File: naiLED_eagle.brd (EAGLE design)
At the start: 12.4 x 12.7 mm, 9 parts, among them IC1 TCS3414, U2 24LC00T-I/OT, U3 ATTINY25-20SSU

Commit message: miniSK led
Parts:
- removed LED1: LED_RGB3, dp_devices:RGBLED
- added U$1: SK6812MINI, pimoroni-optoelectronics:LED-3535
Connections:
- net D1/PWM/MISO: no longer LED1.AG
- net D3/A3: no longer LED1.AR
- net D4/PWM: no longer LED1.AB
- net GND: now also U$1.1; no longer LED1.CB, LED1.CG, LED1.CR
- net VCC: now also U$1.3
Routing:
- net VCC: track 37.9 -> 39.3 mm
- net D4/PWM: track 18.7 -> 18.0 mm
- net GND: vias 5 -> 1
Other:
- board text removed: "LED"

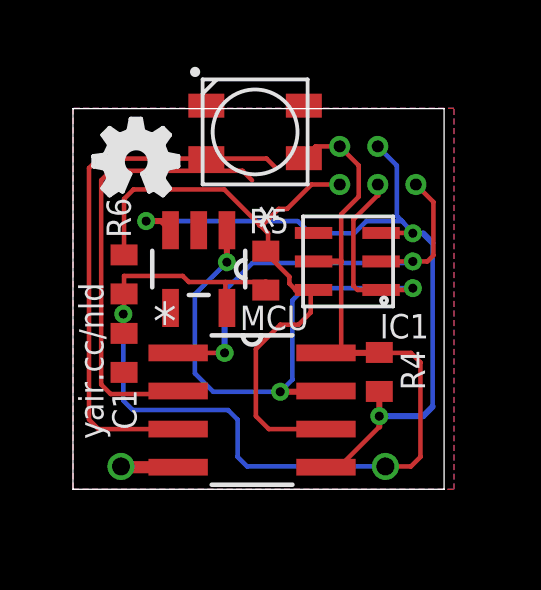
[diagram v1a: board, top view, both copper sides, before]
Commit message: changed attiny25 footprint to 85, ripup
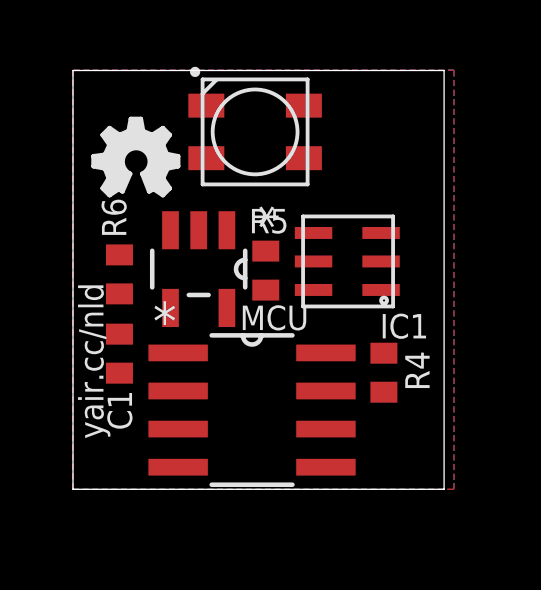
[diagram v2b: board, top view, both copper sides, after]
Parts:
- moved R4 0.15 mm to (10.4, 3.89)
- moved C1 0.15 mm to (1.55, 4.52)
- moved R6 0.15 mm to (1.55, 7.16)
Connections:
- net D4/PWM: now also U$1.2
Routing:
- net VCC: track 39.3 -> 0.00 mm, vias 3 -> 0
- net D0/PWM/MOSI/SDA: track 26.0 -> 0.00 mm, vias 4 -> 0
- net D2/A1/SCK/SCL: track 23.1 -> 0.00 mm, vias 4 -> 0
- net D1/PWM/MISO: track 21.4 -> 0.00 mm, vias 1 -> 0
- net D4/PWM: track 18.0 -> 0.00 mm
- net D3/A3: track 14.9 -> 0.00 mm
- net D5/A0/RESET: track 14.8 -> 0.00 mm, vias 3 -> 0
- net GND: track 1.50 -> 0.00 mm, vias 1 -> 0
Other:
- board size 12.4 x 12.7 mm -> 12.4 x 14 mm

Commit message: routing mid
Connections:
- removed net D5/A0/RESET: IC1.P$2, U3.1
- net D3/A3: now also IC1.P$2
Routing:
- net D0/PWM/MOSI/SDA: track 0.00 -> 25.9 mm
- net D2/A1/SCK/SCL: track 0.00 -> 15.8 mm
- net D4/PWM: track 0.00 -> 12.2 mm, vias 0 -> 2
- net VCC: track 0.00 -> 10.9 mm
- net GND: track 0.00 -> 10.1 mm
- net D1/PWM/MISO: track 0.00 -> 6.97 mm, vias 0 -> 2
- net D3/A3: track 0.00 -> 6.18 mm

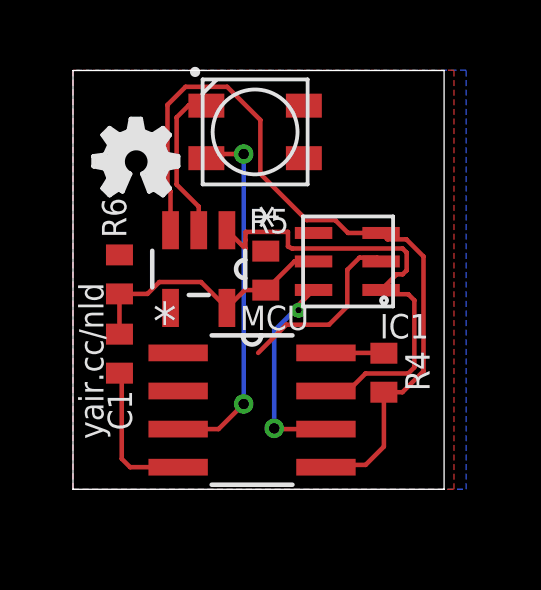
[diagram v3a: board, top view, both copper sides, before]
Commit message: ripup all, added vias to attiny
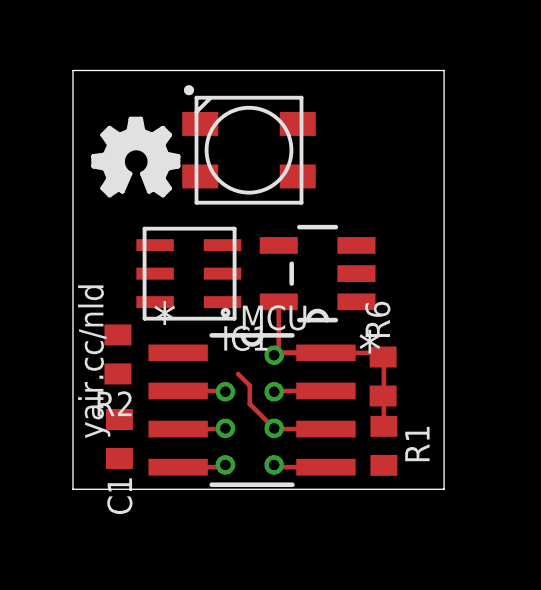
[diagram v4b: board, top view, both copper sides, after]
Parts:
- removed R4, R5: (no value), dp_devices:R402
- added R1, R2: (no value), dp_devices:R402
- moved R6 9.42 mm to (10.3, 3.76)
- moved IC1 5.30 mm to (3.89, 7.19)
- moved U2 3.97 mm to (8.15, 7.19), turned to 180 degrees
- moved C1 2.84 mm to (1.55, 1.68)
- moved U$1 0.64 mm to (5.87, 11.3)
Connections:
- new net NC: U3.1
- net D0/PWM/MOSI/SDA: now also R1.1; no longer R4.1
- net D1/PWM/MISO: now also R2.1; no longer R5.1
- net VCC: now also R1.2, R2.2; no longer R4.2, R5.2
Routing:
- net D0/PWM/MOSI/SDA: track 25.9 -> 1.80 mm, vias 0 -> 1
- net D2/A1/SCK/SCL: track 15.8 -> 1.75 mm, vias 0 -> 1
- net D4/PWM: track 12.2 -> 1.60 mm, vias 2 -> 1
- net GND: track 10.1 -> 1.65 mm, vias 0 -> 1
- net D3/A3: track 6.18 -> 1.60 mm, vias 0 -> 1
- net D1/PWM/MISO: track 6.97 -> 4.07 mm, vias 2 -> 1
- net VCC: track 10.9 -> 9.46 mm, vias 0 -> 1
- removed copper zone on layer 1, net GND
- removed copper zone on layer 16, net GND

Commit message: mem docs
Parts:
- removed C1: (no value), dp_devices:C402
- removed IC1: TCS3414, yair_r:DFN-6PIN
- removed R6: (no value), dp_devices:R402
- added C2: (no value), naiLED_eagle:C402
- added U$2: VEML6040, naiLED_eagle:4-TFLGA
- R1, R2: device dp_devices:R402 -> naiLED_eagle:R402
- U$1: device pimoroni-optoelectronics:LED-3535 -> naiLED_eagle:LED-3535
- U2: device Microchip-24LCxxx:SOT95P290X145-5N -> naiLED_eagle:SOT95P290X145-5N
- U3: value ATTINY25-20SSU -> ATTINY85-20SU; device yair_r:SOIC127P600X175-8N -> naiLED_eagle:SOIC127P798X216-8N
- moved R2 9.93 mm to (9.70, 10.1), turned to 302 degrees
- moved U$1 4.27 mm to (4.04, 7.44)
- moved R1 1.36 mm to (11.6, 2.06)
- moved U2 0.97 mm to (9.12, 7.24), turned to 0 degrees
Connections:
- net D0/PWM/MOSI/SDA: now also U$2.2; no longer IC1.P$3
- net D1/PWM/MISO: no longer IC1.P$4, R2.1, R6.2
- net D2/A1/SCK/SCL: now also R2.1, U$2.3; no longer IC1.P$1
- net D3/A3: no longer IC1.P$2
- net GND: now also C2.1, U$2.1; no longer C1.2, IC1.P$6
- net VCC: now also C2.2, U$2.4; no longer C1.1, IC1.P$5, R6.1
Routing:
- net VCC: track 9.46 -> 0.00 mm, vias 1 -> 0
- net D1/PWM/MISO: track 4.07 -> 0.00 mm, vias 1 -> 0
- net D0/PWM/MOSI/SDA: track 1.80 -> 0.00 mm, vias 1 -> 0
- net D2/A1/SCK/SCL: track 1.75 -> 0.00 mm, vias 1 -> 0
- net GND: track 1.65 -> 0.00 mm, vias 1 -> 0
- net D3/A3: track 1.60 -> 0.00 mm, vias 1 -> 0
- net D4/PWM: track 1.60 -> 0.00 mm, vias 1 -> 0

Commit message: new memory
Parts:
- removed U2: 24LC00T-I/OT, naiLED_eagle:SOT95P290X145-5N
- added U1: AT24C256C-MAHL-T, naiLED_eagle:8MA2
- moved R1 4.21 mm to (9.37, 5.64), turned to 0 degrees
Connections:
- net D0/PWM/MOSI/SDA: now also U1.5; no longer U2.3
- net D2/A1/SCK/SCL: now also U1.6; no longer U2.1
- net GND: now also U1.1, U1.2, U1.3, U1.4; no longer U2.2
- net VCC: now also U1.8; no longer U2.5
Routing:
- net GND: track 0.00 -> 24.2 mm, vias 0 -> 2
- net D0/PWM/MOSI/SDA: track 0.00 -> 18.6 mm, vias 0 -> 2
- net VCC: track 0.00 -> 17.7 mm, vias 0 -> 2
- net D2/A1/SCK/SCL: track 0.00 -> 16.7 mm, vias 0 -> 1
- net D4/PWM: track 0.00 -> 7.44 mm, vias 0 -> 1

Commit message: layout, meh
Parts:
- moved U1 7.62 mm to (1.22, 7.47), turned to 90 degrees
- moved E$1 6.26 mm to (6.93, 10.1)
- moved C2 2.97 mm to (5.05, 11.5), turned to 0 degrees
- moved R2 2.62 mm to (8.37, 7.84), turned to 0 degrees
- moved R1 1.19 mm to (8.46, 6.40)
- moved U3 1.07 mm to (4.90, 2.64)
- moved U$1 0.91 mm to (4.95, 7.44)
- moved U$2 0.15 mm to (5.08, 10.2)
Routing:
- net GND: track 24.2 -> 18.7 mm, vias 2 -> 1
- net D2/A1/SCK/SCL: track 16.7 -> 21.1 mm, vias 1 -> 4
- net VCC: track 17.7 -> 21.1 mm, vias 2 -> 1
- net D0/PWM/MOSI/SDA: track 18.6 -> 17.6 mm, vias 2 -> 3
- net D4/PWM: track 7.44 -> 6.50 mm, vias 1 -> 2
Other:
- board size 12.4 x 14 mm -> 9.9 x 14 mm

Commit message: auditing
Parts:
- moved E$1 2.96 mm to (6.32, 7.21), flipped to the bottom
- moved C2 2.88 mm to (7.70, 10.3), turned to 315 degrees
- moved R2 0.76 mm to (8.37, 8.60)
- moved U$1 0.76 mm to (4.95, 8.20)
- moved U3 0.76 mm to (4.90, 3.40)
- moved R1 0.76 mm to (8.46, 7.16)
- moved U1 0.76 mm to (1.22, 8.23)
- moved U$2 0.76 mm to (5.08, 11.0)
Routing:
- net VCC: track 21.1 -> 27.1 mm, vias 1 -> 3
- net GND: track 18.7 -> 24.3 mm, vias 1 -> 3
- net D2/A1/SCK/SCL: track 21.1 -> 24.8 mm, vias 4 -> 5
- net D0/PWM/MOSI/SDA: track 17.6 -> 19.4 mm, vias 3 -> 4
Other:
- board size 9.9 x 14 mm -> 9.9 x 12.3 mm
- board text removed: "MCU"
